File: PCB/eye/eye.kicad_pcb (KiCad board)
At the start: 2 copper layers, 6 parts, among them J1 LH128, U1 RP2040, U2 W25Q32JVSS

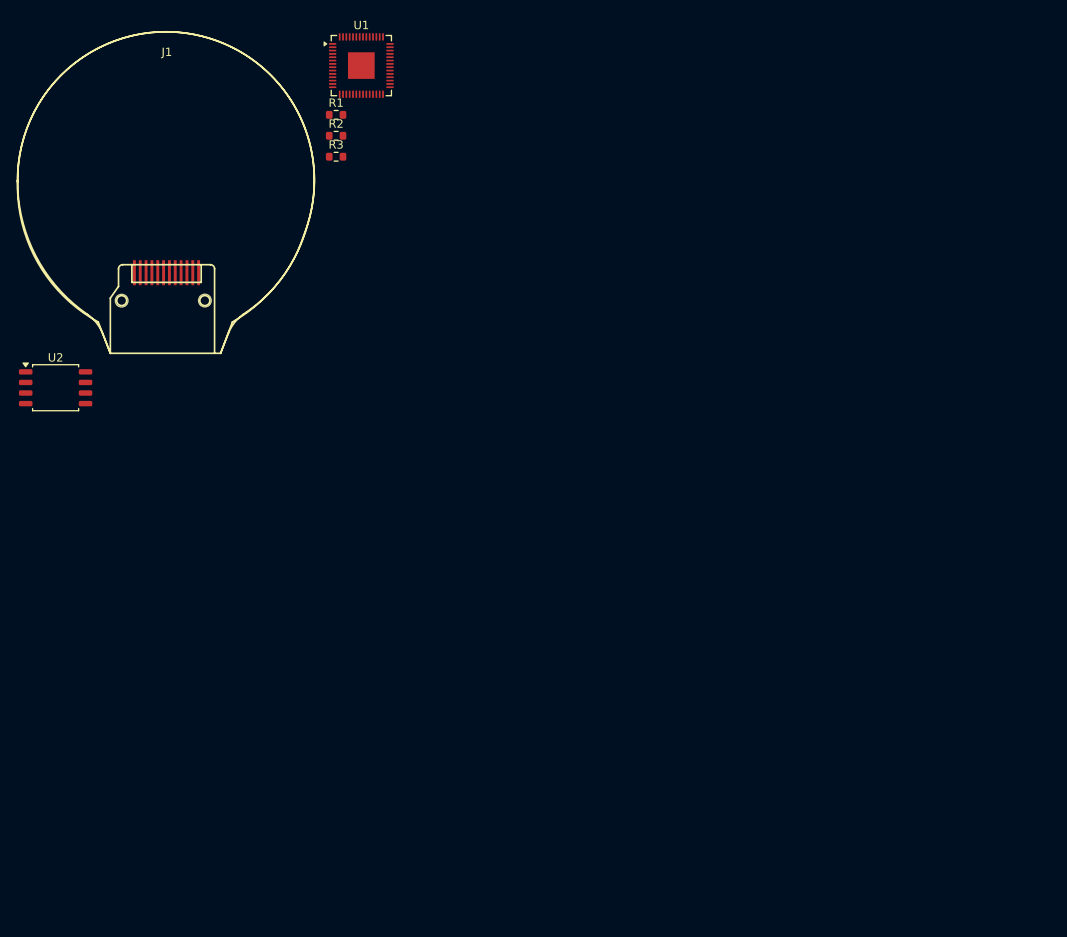
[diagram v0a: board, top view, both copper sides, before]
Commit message: finish placement
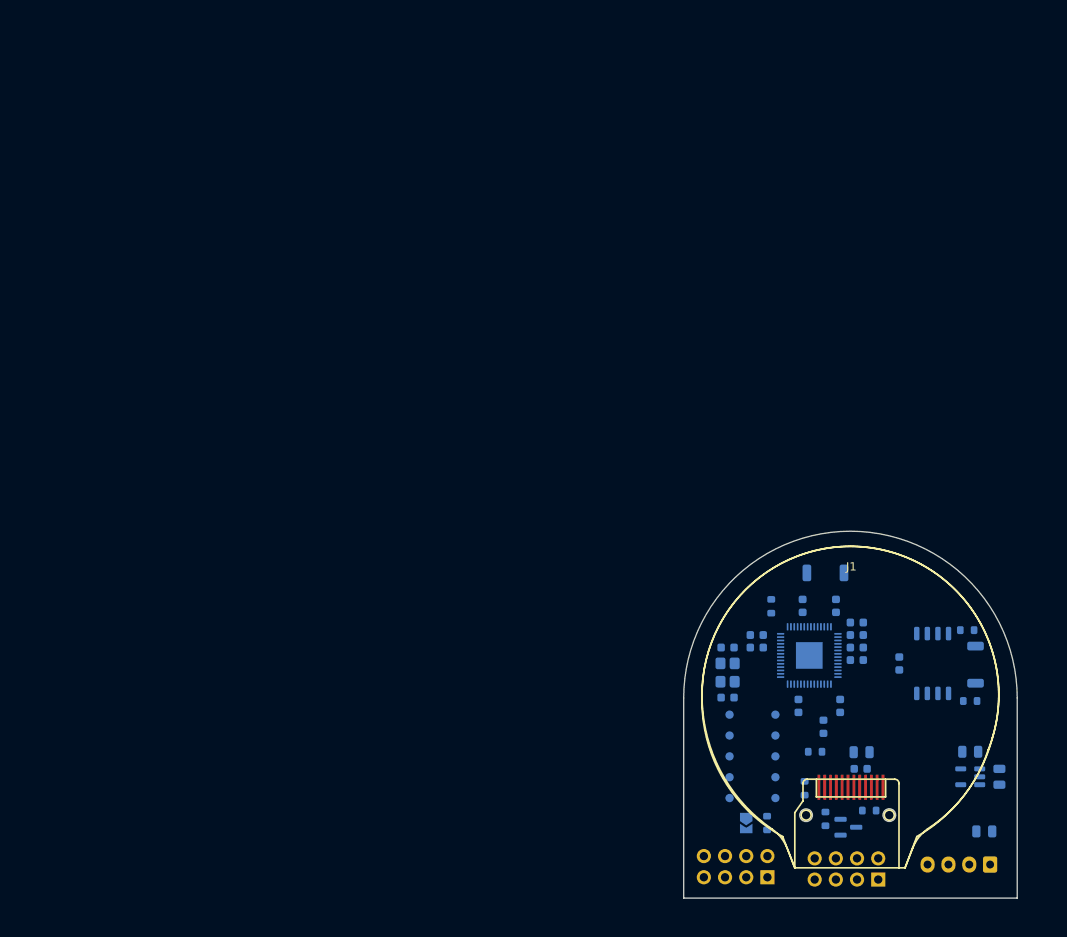
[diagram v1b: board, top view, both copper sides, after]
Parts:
- added C1: 0.1uF, Capacitor_SMD:C_0603_1608Metric, B.Cu at (105.9, 75.9)
- added C10: 0.1uF, Capacitor_SMD:C_0603_1608Metric, B.Cu at (88.8, 74.0)
- added C11: 0.1uF, Capacitor_SMD:C_0603_1608Metric, B.Cu at (94.3, 69.0)
- added C12: 0.1uF, Capacitor_SMD:C_0603_1608Metric, B.Cu at (98.8, 81.0)
- added C13: 0.1uF, Capacitor_SMD:C_0603_1608Metric, B.Cu at (93.8, 81.0)
- added C14: 0.1uF, Capacitor_SMD:C_0603_1608Metric, B.Cu at (88.8, 72.5)
- added C15: 0.1uF, Capacitor_SMD:C_0603_1608Metric, B.Cu at (100.8, 75.5)
- added C16: 1uF, Capacitor_SMD:C_0603_1608Metric, B.Cu at (98.3, 69.0)
- added C17: 1uF, Capacitor_SMD:C_0603_1608Metric, B.Cu at (101.2, 88.5)
- added C18: 1uF, Capacitor_SMD:C_0603_1608Metric, B.Cu at (100.8, 72.5)
- added C2: 33pF, Capacitor_SMD:C_0603_1608Metric, B.Cu at (85.3, 74.0)
- added C3: 33pF, Capacitor_SMD:C_0603_1608Metric, B.Cu at (85.3, 80.0)
- added C4: 10uF, Capacitor_SMD:C_0805_2012Metric, B.Cu at (116.0, 96.0)
- added C5: 10uF, Capacitor_SMD:C_0805_2012Metric, B.Cu at (114.4, 86.5)
- added C6: 10uF, Capacitor_SMD:C_0805_2012Metric, B.Cu at (117.9, 89.5)
- added C7: 10uF, Capacitor_SMD:C_0805_2012Metric, B.Cu at (101.3, 86.5)
- added C8: 0.1uF, Capacitor_SMD:C_0603_1608Metric, B.Cu at (100.8, 71.0)
- added C9: 0.1uF, Capacitor_SMD:C_0603_1608Metric, B.Cu at (100.8, 74.0)
- added D1: LED, LED_SMD:LED_0603_1608Metric, B.Cu at (96.8, 83.5)
- added G10: TestPoint, TestPoint:TestPoint_Pad_D1.0mm, B.Cu at (91.0, 82.0)
- added G11: TestPoint, TestPoint:TestPoint_Pad_D1.0mm, B.Cu at (85.5, 92.0)
- added G12: TestPoint, TestPoint:TestPoint_Pad_D1.0mm, B.Cu at (85.5, 89.5)
- added G13: TestPoint, TestPoint:TestPoint_Pad_D1.0mm, B.Cu at (85.5, 87.0)
- added G14: TestPoint, TestPoint:TestPoint_Pad_D1.0mm, B.Cu at (85.5, 84.5)
- added G15: TestPoint, TestPoint:TestPoint_Pad_D1.0mm, B.Cu at (85.5, 82.0)
- added G6: TestPoint, TestPoint:TestPoint_Pad_D1.0mm, B.Cu at (91.0, 92.0)
- added G7: TestPoint, TestPoint:TestPoint_Pad_D1.0mm, B.Cu at (91.0, 89.5)
- added G8: TestPoint, TestPoint:TestPoint_Pad_D1.0mm, B.Cu at (91.0, 87.0)
- added G9: TestPoint, TestPoint:TestPoint_Pad_D1.0mm, B.Cu at (91.0, 84.5)
- added J2: Conn_01x04, Connector_JST:JST_XH_B4B-XH-A_1x04_P2.50mm_Vertical, B.Cu at (116.8, 100.0)
- added J3: Conn_01x08, Connector_PinHeader_2.54mm:PinHeader_2x04_P2.54mm_Vertical, B.Cu at (90.0, 101.5)
- added J4: Conn_01x08, Connector_PinHeader_2.54mm:PinHeader_2x04_P2.54mm_Vertical, B.Cu at (103.3, 101.8)
- added JP1: SolderJumper_2_Open, Jumper:SolderJumper-2_P1.3mm_Open_TrianglePad1.0x1.5mm, B.Cu at (87.5, 95.0)
- added Q1: AO3400A, Package_TO_SOT_SMD:SOT-23, B.Cu at (99.8, 95.5)
- added R4: 10k, Resistor_SMD:R_0603_1608Metric, B.Cu at (90.5, 69.0)
- added R5: 100k, Resistor_SMD:R_0603_1608Metric, B.Cu at (97.0, 94.5)
- added R6: 22, Resistor_SMD:R_0603_1608Metric, B.Cu at (102.2, 93.5)
- added R7: 100, Resistor_SMD:R_0603_1608Metric, B.Cu at (90.0, 95.0)
- added R8: 1k, Resistor_SMD:R_0603_1608Metric, B.Cu at (95.8, 86.5)
- added SW1: SW_Push, Button_Switch_SMD:SW_SPST_TS-1088-xR025, B.Cu at (115.0, 76.0)
- added SW2: SW_Push, Button_Switch_SMD:SW_SPST_TS-1088-xR025, B.Cu at (97.0, 65.0)
- added U3: AP2112K-3.3, Package_TO_SOT_SMD:SOT-23-5, B.Cu at (114.4, 89.5)
- added Y1: 12MHz, Crystal:Crystal_SMD_3225-4Pin_3.2x2.5mm, B.Cu at (85.3, 77.0)
- R1: value 2 -> 100; moved to B.Cu
- R2, R3, U1, U2: moved to B.Cu
- moved U2 110.3 mm to (109.9, 75.9), turned to 90 degrees
- moved J1 102.7 mm to (100.0, 80.0)
- moved R3 100.2 mm to (114.4, 80.4)
- moved R1 98.4 mm to (94.5, 90.8), turned to -90 degrees
- moved R2 96.1 mm to (114.0, 71.9), turned to 180 degrees
- moved U1 88.8 mm to (95.1, 74.9), turned to 90 degrees
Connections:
- net Net-(U1-QSPI_SD0) renamed /QSPI_SD0
- net Net-(U1-QSPI_SD1) renamed /QSPI_SD1
- net Net-(U1-QSPI_SD2) renamed /QSPI_SD2
- net Net-(U1-QSPI_SD3) renamed /QSPI_SD3
- J1 pad 10: SDA -> MOSI
- J1 pad 11: RES -> RST
- J1 pad 2: Net-(J1-Pin_2) -> BL
- J1 pad 9: SCL -> SCK
- R1 pad 1: GND -> BL_PIN
- R1 pad 2: Net-(J1-Pin_2) -> Net-(Q1-G)
- R2 pad 1: Net-(U1-~{QSPI_SS}) -> /QSPI_SS
- R3 pad 1: Net-(U1-~{QSPI_SS}) -> /QSPI_SS
- U1 pad 11: unconnected-(U1-GPIO8-Pad11) -> Net-(U1-GPIO8)
- U1 pad 12: unconnected-(U1-GPIO9-Pad12) -> Net-(U1-GPIO9)
- U1 pad 13: unconnected-(U1-GPIO10-Pad13) -> Net-(U1-GPIO10)
- U1 pad 14: unconnected-(U1-GPIO11-Pad14) -> Net-(U1-GPIO11)
- U1 pad 15: unconnected-(U1-GPIO12-Pad15) -> Net-(U1-GPIO12)
- U1 pad 16: unconnected-(U1-GPIO13-Pad16) -> Net-(U1-GPIO13)
- U1 pad 17: unconnected-(U1-GPIO14-Pad17) -> Net-(U1-GPIO14)
- U1 pad 18: unconnected-(U1-GPIO15-Pad18) -> Net-(U1-GPIO15)
- U1 pad 2: unconnected-(U1-GPIO0-Pad2) -> TX
- U1 pad 20: unconnected-(U1-XIN-Pad20) -> Net-(U1-XIN)
- U1 pad 21: unconnected-(U1-XOUT-Pad21) -> Net-(U1-XOUT)
- U1 pad 24: unconnected-(U1-SWCLK-Pad24) -> SWCLK
- U1 pad 25: unconnected-(U1-SWDIO-Pad25) -> SWDIO
- U1 pad 26: unconnected-(U1-RUN-Pad26) -> RUN
- U1 pad 28: unconnected-(U1-GPIO17-Pad28) -> CS
- U1 pad 29: unconnected-(U1-GPIO18-Pad29) -> SCK
- U1 pad 3: unconnected-(U1-GPIO1-Pad3) -> RX
- U1 pad 30: unconnected-(U1-GPIO19-Pad30) -> MOSI
- U1 pad 31: unconnected-(U1-GPIO20-Pad31) -> DC
- U1 pad 32: unconnected-(U1-GPIO21-Pad32) -> RST
- U1 pad 34: unconnected-(U1-GPIO22-Pad34) -> BL_PIN
- U1 pad 4: unconnected-(U1-GPIO2-Pad4) -> Net-(D1-A)
- U1 pad 52: /QSPI_SS -> /QSPI_SCLK
- U1 pad 56: Net-(U1-~{QSPI_SS}) -> /QSPI_SS
- U1 pad 6: unconnected-(U1-GPIO4-Pad6) -> SDA
- U1 pad 7: unconnected-(U1-GPIO5-Pad7) -> SCL
- U1 pad 8: unconnected-(U1-GPIO6-Pad8) -> Net-(U1-GPIO6)
- U1 pad 9: unconnected-(U1-GPIO7-Pad9) -> Net-(U1-GPIO7)
- U2 pad 1: Net-(U1-~{QSPI_SS}) -> /QSPI_SS
- U2 pad 4: unconnected-(U2-GND-Pad4) -> GND
- U2 pad 6: /QSPI_SS -> /QSPI_SCLK
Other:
- board outline added: 40 x 44 mm

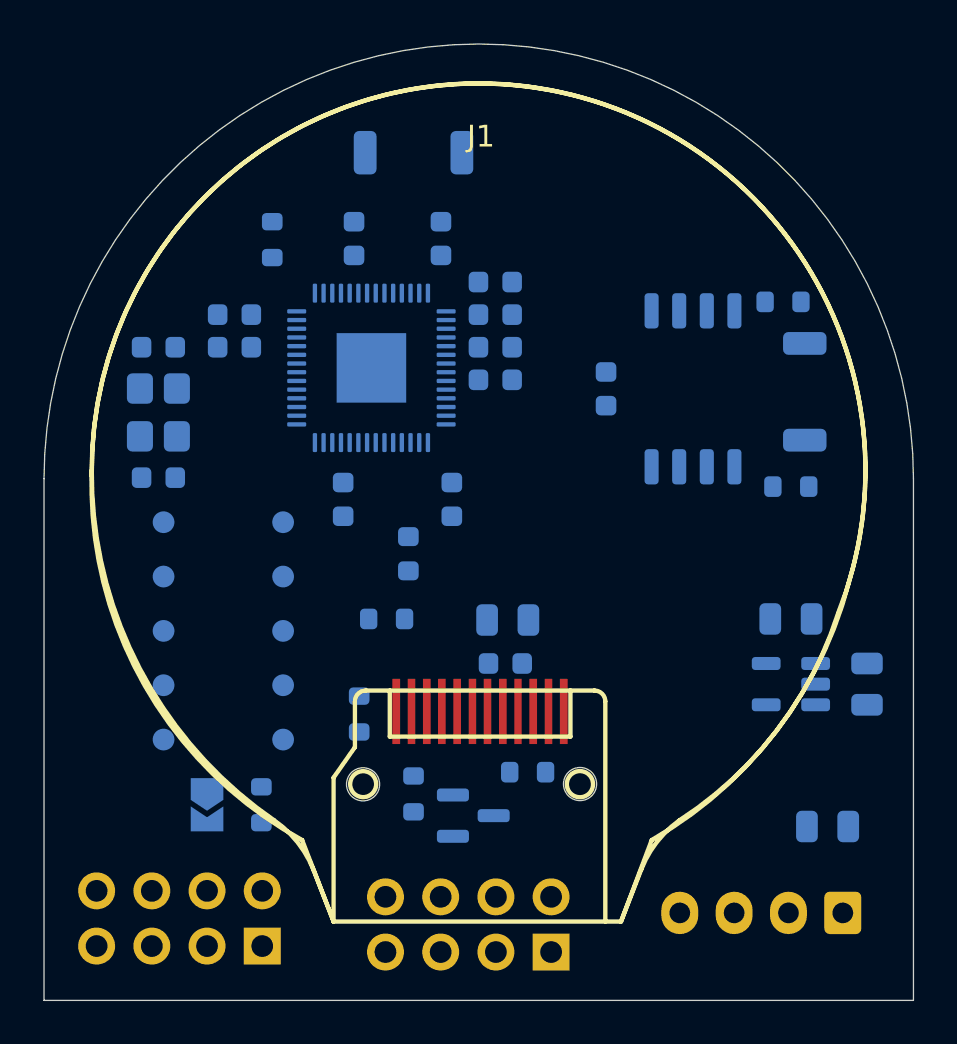
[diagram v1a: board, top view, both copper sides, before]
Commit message: mostly routed
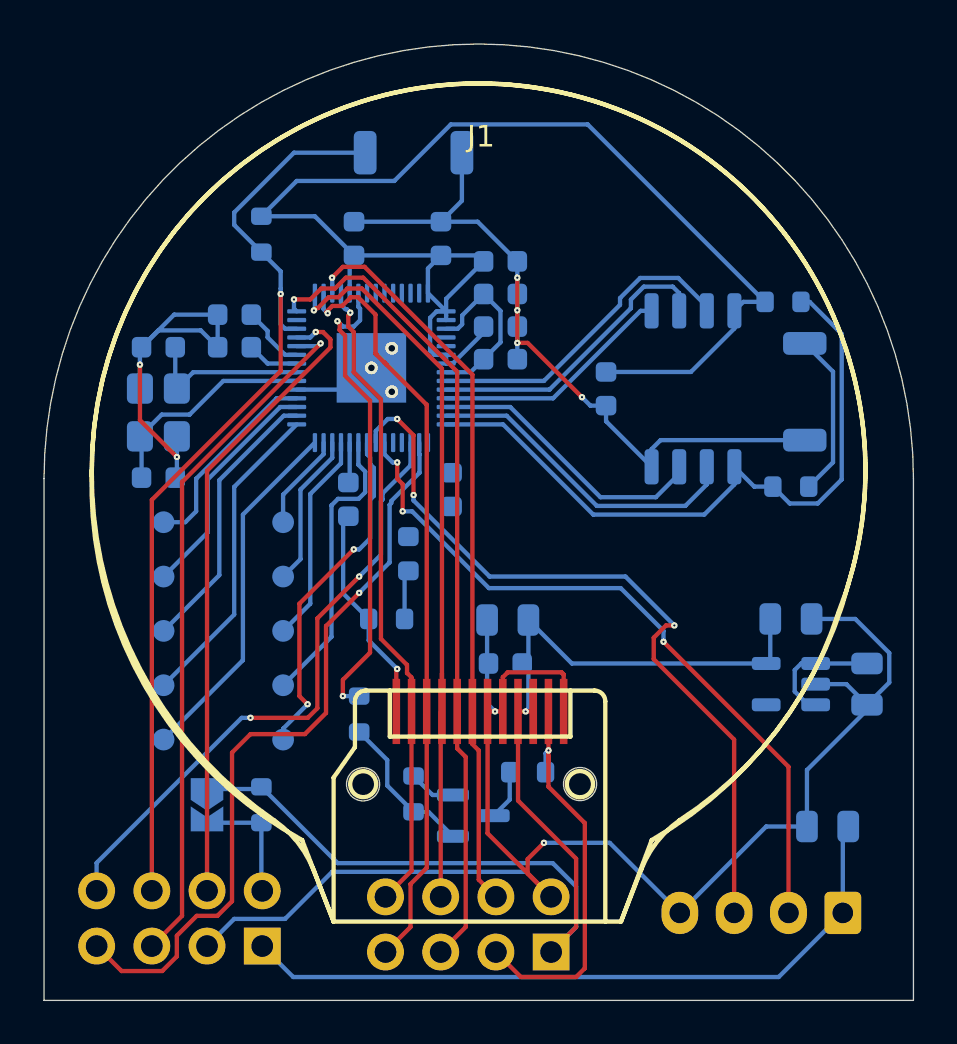
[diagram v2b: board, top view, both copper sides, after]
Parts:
- moved C15 0.98 mm to (101.0, 74.5)
- moved C18 0.98 mm to (101.0, 71.5)
- moved C8 0.98 mm to (101.0, 70.0)
- moved C9 0.98 mm to (101.0, 73.0)
- moved R4 0.56 mm to (90.0, 68.8)
- moved C12 0.45 mm to (98.8, 80.5)
- moved C13 0.24 mm to (94.0, 81.0)
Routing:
- net GND: track 0.00 -> 144.6 mm, vias 0 -> 12
- net +3.3V: track 0.00 -> 121.4 mm, vias 0 -> 1
- net RUN: track 0.00 -> 43.9 mm, vias 0 -> 1
- net +5V: track 0.00 -> 38.3 mm
- net CS: track 0.00 -> 37.7 mm, vias 0 -> 1
- net SCL: track 0.00 -> 35.6 mm, vias 0 -> 3
- net MOSI: track 0.00 -> 35.1 mm, vias 0 -> 1
- net TX: track 0.00 -> 34.7 mm, vias 0 -> 1
- net SCK: track 0.00 -> 34.7 mm, vias 0 -> 1
- net DC: track 0.00 -> 33.9 mm, vias 0 -> 1
- net SDA: track 0.00 -> 33.3 mm, vias 0 -> 3
- net SWCLK: track 0.00 -> 32.2 mm, vias 0 -> 1
- net /QSPI_SS: track 0.00 -> 31.6 mm
- net RST: track 0.00 -> 29.7 mm, vias 0 -> 1
- net SWDIO: track 0.00 -> 29.5 mm, vias 0 -> 1
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
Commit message: bigger vias
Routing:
- net BL_PIN: track 21.7 -> 65.1 mm
- net +3.3V: track 121.4 -> 154.1 mm, vias 1 -> 6
- net +1V1: track 11.3 -> 21.9 mm, vias 0 -> 2
- net SWCLK: track 32.2 -> 31.0 mm
- net RST: track 29.7 -> 30.6 mm
- net DC: track 33.9 -> 34.8 mm
- net SCK: track 34.7 -> 35.4 mm
- net GND: track 144.6 -> 144.8 mm, vias 12 -> 10

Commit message: continue routing
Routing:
- net GND: track 144.8 -> 217.0 mm, vias 10 -> 13
- net +5V: track 38.3 -> 51.1 mm, vias 0 -> 2
- net Net-(D1-A): track 0.00 -> 9.01 mm, vias 0 -> 2
- net SCL: track 35.2 -> 37.5 mm

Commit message: fix all DRC errors
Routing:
- net GND: track 217.0 -> 221.7 mm

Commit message: finish Eye PCB
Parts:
- renumbered SW1 to BOOT1, SW2 to RUN1
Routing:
- net GND: track 221.7 -> 235.1 mm, vias 13 -> 14
- net +5V: track 51.1 -> 52.3 mm, vias 2 -> 3
- added copper zone on B.Cu, net +3.3V
- added copper zone on B.Cu, net +5V
- added copper zone on F.Cu, net +5V
- added copper zone on B.Cu, net GND
- added copper zone on F.Cu, net GND
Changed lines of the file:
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@@
 		(descr "SMD Tactile Switch, 3.9x3x2.5 mm, https://lcsc.com/datasheet/lcsc_datasheet_2504101957_XUNPU-TS-1088-AR02016_C720477.pdf")
 		(tags "Tactile Switch")
-		(property "Reference" "SW2"
+		(property "Reference" "RUN1"
 			(at 0 2.5 0)
 			(layer "B.SilkS")
@@
 		(descr "SMD Tactile Switch, 3.9x3x2.5 mm, https://lcsc.com/datasheet/lcsc_datasheet_2504101957_XUNPU-TS-1088-AR02016_C720477.pdf")
 		(tags "Tactile Switch")
-		(property "Reference" "SW1"
+		(property "Reference" "BOOT1"
 			(at 0 2.65 90)
 			(layer "B.SilkS")
@@
 			(layers "B.Cu" "B.Mask" "B.Paste")
 			(roundrect_rratio 0.2380952381)
-			(net "Net-(R3-Pad2)")
+			(net "Net-(BOOT1-Pad2)")
 			(pinfunction "2_2")
 			(pintype "passive")
@@
 			(layers "B.Cu" "B.Mask" "B.Paste")
 			(roundrect_rratio 0.25)
-			(net "Net-(R3-Pad2)")
+			(net "Net-(BOOT1-Pad2)")
 			(pintype "passive")
 		)
@@
 	)
 	(segment
-		(start 96.2078 88.7922)
-		(end 96.2078 90.7061)
-		(width 0.2)
-		(layer "F.Cu")
-		(net "GND")
-	)
-	(segment
 		(start 102.875 96.875)
 		(end 102.25 97.5)
@@
 	)
 	(segment
+		(start 96.2078 90.7061)
+		(end 96.2078 90.1078)
+		(width 0.2)
+		(layer "F.Cu")
+		(net "GND")
+	)
+	(segment
 		(start 103.8078 88.9061)
 		(end 103.9078 89.0061)
@@
 	)
 	(segment
+		(start 100.4078 87.5)
+		(end 100.4078 86.8078)
+		(width 0.2)
+		(layer "F.Cu")
+		(net "GND")
+	)
+	(segment
 		(start 101.775 73.75)
 		(end 102.25 73.75)
@@
 	)
 	(segment
-		(start 101.6 84.920244)
-		(end 101.6 81.3)
+		(start 96.2078 89.2578)
+		(end 95.7 88.75)
 		(width 0.2)
 		(layer "F.Cu")
@@
 	)
 	(segment
-		(start 95.7 88.75)
-		(end 96.1656 88.75)
+		(start 101.6 84.920244)
+		(end 101.6 81.3)
 		(width 0.2)
 		(layer "F.Cu")
@@
 	)
 	(segment
-		(start 96.1656 88.75)
-		(end 96.2078 88.7922)
+		(start 101.3328 88.9061)
+		(end 103.8078 88.9061)
 		(width 0.2)
 		(layer "F.Cu")
@@
 	)
 	(segment
-		(start 101.3328 88.9061)
-		(end 103.8078 88.9061)
+		(start 100.4078 90.7061)
+		(end 100.4078 87.5)
 		(width 0.2)
 		(layer "F.Cu")
@@
 	)
 	(segment
+		(start 96.2078 90.7061)
+		(end 96.2078 89.2578)
+		(width 0.2)
+		(layer "F.Cu")
+		(net "GND")
+	)
+	(segment
 		(start 100.4078 96.3128)
 		(end 100.4078 90.7061)
@@
 	)
 	(segment
+		(start 96.2078 90.1078)
+		(end 94.5 88.4)
+		(width 0.2)
+		(layer "F.Cu")
+		(net "GND")
+	)
+	(segment
 		(start 104.75 81.85)
 		(end 104.75 76.25)
@@
 	)
 	(via
+		(at 100.4078 87.5)
+		(size 0.45)
+		(drill 0.3)
+		(layers "F.Cu" "B.Cu")
+		(net "GND")
+	)
+	(via
 		(at 101.6 81.3)
 		(size 0.5)
@@
 	)
 	(segment
+		(start 103.33 99.235)
+		(end 102.465 100.1)
+		(width 0.2)
+		(layer "B.Cu")
+		(net "GND")
+	)
+	(segment
 		(start 106.025 96.75)
 		(end 109.25 99.975)
@@
 	)
 	(segment
+		(start 98.8125 94.55)
+		(end 98.8125 95.003052)
+		(width 0.2)
+		(layer "B.Cu")
+		(net "GND")
+	)
+	(segment
 		(start 86.159692 78.05)
 		(end 86.1125 78.05)
@@
 	)
 	(segment
+		(start 100.409448 96.6)
+		(end 102.6 96.6)
+		(width 0.2)
+		(layer "B.Cu")
+		(net "GND")
+	)
+	(segment
 		(start 93.7625 81.725)
 		(end 93.7625 85.275)
@@
 	)
 	(segment
+		(start 102.465 100.1)
+		(end 102.2 100.1)
+		(width 0.2)
+		(layer "B.Cu")
+		(net "GND")
+	)
+	(segment
 		(start 107.9525 78.637501)
 		(end 107.9525 79.45)
@@
 	)
 	(segment
+		(start 102.6 96.6)
+		(end 102.875 96.875)
+		(width 0.2)
+		(layer "B.Cu")
+		(net "GND")
+	)
+	(segment
 		(start 101.6 81.3)
 		(end 103.5 81.3)
@@
 	)
 	(segment
+		(start 98.8125 95.003052)
+		(end 100.409448 96.6)
+		(width 0.2)
+		(layer "B.Cu")
+		(net "GND")
+	)
+	(segment
 		(start 94.2625 68.175)
 		(end 98.2625 68.175)
@@
 		(start 113.225 88.5)
 		(end 104.285 88.5)
-		(width 0.2)
+		(width 0.5)
 		(layer "B.Cu")
 		(net "+3.3V")
@@
 		(start 113.4125 86.45)
 		(end 113.4125 88.3125)
-		(width 0.2)
+		(width 1)
 		(layer "B.Cu")
 		(net "+3.3V")
@@
 		(start 104.285 88.5)
 		(end 102.285 86.5)
-		(width 0.2)
+		(width 0.5)
 		(layer "B.Cu")
 		(net "+3.3V")
@@
 		(net "+5V")
 	)
+	(via
+		(at 115.4 91.6)
+		(size 0.45)
+		(drill 0.3)
+		(layers "F.Cu" "B.Cu")
+		(free yes)
+		(net "+5V")
+	)
 	(segment
 		(start 116.752705 94.802705)
@@
 	)
 	(segment
+		(start 115.5 90.4)
+		(end 115.5 91.5)
+		(width 0.2)
+		(layer "B.Cu")
+		(net "+5V")
+	)
+	(segment
 		(start 116.752705 95.399999)
 		(end 116.752705 94.802705)
@@
 	)
 	(segment
+		(start 115.5 91.5)
+		(end 115.4 91.6)
+		(width 0.2)
+		(layer "B.Cu")
+		(net "+5V")
+	)
+	(segment
 		(start 91.465 102.925)
 		(end 113.8 102.925)
@@
 	)
 	(segment
-		(start 115.1825 80.3625)
-		(end 116.3 79.245)
-		(width 0.2)
-		(layer "B.Cu")
-		(net "Net-(R3-Pad2)")
-	)
-	(segment
-		(start 116.3 75.075)
-		(end 115 73.775)
-		(width 0.2)
-		(layer "B.Cu")
-		(net "Net-(R3-Pad2)")
-	)
-	(segment
-		(start 116.3 79.245)
-		(end 116.3 75.075)
-		(width 0.2)
-		(layer "B.Cu")
-		(net "Net-(R3-Pad2)")
-	)
-	(segment
 		(start 92.4625 78.3375)
 		(end 89.15 81.65)
@@
 		(net "Net-(U1-GPIO15)")
 	)
+	(segment
+		(start 115.1825 80.3625)
+		(end 116.3 79.245)
+		(width 0.2)
+		(layer "B.Cu")
+		(net "Net-(BOOT1-Pad2)")
+	)
+	(segment
+		(start 116.3 75.075)
+		(end 115 73.775)
+		(width 0.2)
+		(layer "B.Cu")
+		(net "Net-(BOOT1-Pad2)")
+	)
+	(segment
+		(start 116.3 79.245)
+		(end 116.3 75.075)
+		(width 0.2)
+		(layer "B.Cu")
+		(net "Net-(BOOT1-Pad2)")
+	)
+	(zone
+		(net "+5V")
+		(layers "F.Cu" "B.Cu")
+		(hatch edge 0.5)
+		(priority 1)
+		(connect_pads
+			(clearance 0.5)
+		)
+		(min_thickness 0.2)
+		(fill yes
+			(thermal_gap 0.5)
+			(thermal_bridge_width 0.5)
+			(island_removal_mode 0)
+		)
+		(polygon
+			(pts
+				(xy 119 87) (xy 114.3625 87) (xy 114.6 101.4) (xy 119 101.4)
+			)
+		)
+	)
+	(zone
+		(net "GND")
+		(layers "F.Cu" "B.Cu")
+		(hatch edge 0.5)
+		(connect_pads
+			(clearance 0.5)
+		)
+		(min_thickness 0.25)
+		(fill yes
+			(thermal_gap 0.5)
+			(thermal_bridge_width 0.5)
+			(smoothing chamfer)
+			(radius 0.5)
+			(island_removal_mode 0)
+		)
+		(polygon
+			(pts
+				(xy 78.3 57.1) (xy 78.355295 106.663196) (xy 124 106.3) (xy 123.7 58.1)
+			)
+		)
+	)
+	(zone
+		(net "+3.3V")
+		(layer "B.Cu")
+		(hatch edge 0.5)
+		(priority 2)
+		(connect_pads
+			(clearance 0.5)
+		)
+		(min_thickness 0.2)
+		(fill yes
+			(thermal_gap 0.5)
+			(thermal_bridge_width 0.5)
+			(island_removal_mode 0)
+		)
+		(polygon
+			(pts
+				(xy 87.2 67.5) (xy 112.3 67.604149) (xy 112.3 82.504149) (xy 87.2 82.4)
+			)
+		)
+	)
 	(embedded_fonts no)
